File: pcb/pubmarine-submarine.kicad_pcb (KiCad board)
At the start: 2 copper layers, 150.5 x 100 mm, 68 parts, among them J1 GPIO_IN, J10 RPD, J11 Screw_Terminal_01x08, J12 Screw_Terminal_01x08, J13 ADC_HDR, J14 PWM_HDR, J2 GPIO_OUT, J3 FYL, J4 FYR, J5 FPU, J6 FPD, J7 RPU, J8 RYL, J9 RYR, Q1 AO3400A, Q2 AO3400A, Q3 AO3400A, Q4 AO3400A, Q5 AO3400A, Q6 AO3400A, Q7 AO3400A, Q8 AO3400A, U1 A4950E, U2 A4950E, U3 A4950E, U4 A4950E, U5 TLC5947DAP, U6 MCP3008

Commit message: new PCB
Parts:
- added C10: 0.22uF, Capacitor_SMD:C_0603_1608Metric_Pad1.08x0.95mm_HandSolder, F.Cu at (254.5, 69.8)
- added C11: 100uF, Capacitor_THT:CP_Radial_D6.3mm_P2.50mm, F.Cu at (257.8, 84.5)
- added C9: 100uF, Capacitor_THT:CP_Radial_D6.3mm_P2.50mm, F.Cu at (248.5, 84.5)
- added D10: WS2812B, LED_SMD:LED_WS2812B_PLCC4_5.0x5.0mm_P3.2mm, F.Cu at (271.1, 82.0)
- added D11: WS2812B, LED_SMD:LED_WS2812B_PLCC4_5.0x5.0mm_P3.2mm, F.Cu at (270.9, 91.0)
- added D12: LED, LED_SMD:LED_0603_1608Metric_Pad1.05x0.95mm_HandSolder, F.Cu at (199.0, 79.2)
- added D13: LED, LED_SMD:LED_0603_1608Metric_Pad1.05x0.95mm_HandSolder, F.Cu at (212.2, 79.0)
- added D14: LED, LED_SMD:LED_0603_1608Metric_Pad1.05x0.95mm_HandSolder, F.Cu at (223.9, 79.0)
- added D9: WS2812B, LED_SMD:LED_WS2812B_PLCC4_5.0x5.0mm_P3.2mm, F.Cu at (271.1, 72.5)
- added J15: Servo1, Connector_JST:JST_PH_B3B-PH-K_1x03_P2.00mm_Vertical, F.Cu at (272.5, 114.8)
- added J16: Servo2, Connector_JST:JST_PH_B3B-PH-K_1x03_P2.00mm_Vertical, F.Cu at (272.5, 109.3)
- added J17: Servo3, Connector_JST:JST_PH_B3B-PH-K_1x03_P2.00mm_Vertical, F.Cu at (272.5, 103.8)
- added J18: Servo4, Connector_JST:JST_PH_B3B-PH-K_1x03_P2.00mm_Vertical, F.Cu at (272.5, 98.2)
- added J19: Conn_01x02, Connector_JST:JST_XH_B2B-XH-AM_1x02_P2.50mm_Vertical, F.Cu at (235.9, 63.0)
- added J20: Conn_01x02, Connector_JST:JST_XH_B2B-XH-AM_1x02_P2.50mm_Vertical, F.Cu at (244.7, 63.0)
- added J21: Conn_01x02, Connector_JST:JST_XH_B2B-XH-AM_1x02_P2.50mm_Vertical, F.Cu at (253.4, 63.0)
- added J22: Conn_01x02, Connector_JST:JST_XH_B2B-XH-AM_1x02_P2.50mm_Vertical, F.Cu at (262.4, 63.0)
- added J23: Conn_01x02, Connector_JST:JST_PH_B2B-PH-K_1x02_P2.00mm_Vertical, F.Cu at (178.2, 79.8)
- added J24: Conn_01x02, Connector_JST:JST_PH_B2B-PH-K_1x02_P2.00mm_Vertical, F.Cu at (185.5, 79.8)
- added R21: 1K, Resistor_SMD:R_0603_1608Metric_Pad0.98x0.95mm_HandSolder, F.Cu at (194.8, 79.2)
- added R22: 330, Resistor_SMD:R_0603_1608Metric_Pad0.98x0.95mm_HandSolder, F.Cu at (207.8, 79.0)
- added R23: 330, Resistor_SMD:R_0603_1608Metric_Pad0.98x0.95mm_HandSolder, F.Cu at (219.6, 79.0)
- added SW1: SW_SPDT, Button_Switch_THT:SW_Slide_SPDT_Straight_CK_OS102011MS2Q, F.Cu at (199.1, 75.0)
- added SW2: SW_SPDT, Button_Switch_THT:SW_Slide_SPDT_Straight_CK_OS102011MS2Q, F.Cu at (211.6, 75.0)
- added SW3: SW_SPDT, Button_Switch_THT:SW_Slide_SPDT_Straight_CK_OS102011MS2Q, F.Cu at (223.7, 75.0)
- C1, C5, C7: value 0.22uF -> 100uF; footprint Capacitor_SMD:C_0603_1608Metric_Pad1.08x0.95mm_HandSolder -> Capacitor_THT:CP_Radial_D6.3mm_P2.50mm
- C2: footprint Capacitor_THT:CP_Radial_D5.0mm_P2.50mm -> Capacitor_THT:CP_Radial_D6.3mm_P2.50mm
- C3: value 0.22uF -> 0.1uF
- C4, C6, C8: value 100uF -> 0.22uF; footprint Capacitor_THT:CP_Radial_D5.0mm_P2.50mm -> Capacitor_SMD:C_0603_1608Metric_Pad1.08x0.95mm_HandSolder
- D1, D2, D3, D4, D5, D6, D7, D8: value D_Schottky -> 1N5822; footprint Diode_SMD:D_0603_1608Metric_Pad1.05x0.95mm_HandSolder -> Diode_SMD:D_0603_1608Metric
- H1: value MountingHole_Pad -> MountingHole; footprint MountingHole:MountingHole_3.2mm_M3_Pad -> MountingHole:MountingHole_2.2mm_M2
- H2, H3: footprint MountingHole:MountingHole_3.2mm_M3 -> MountingHole:MountingHole_2.2mm_M2
- H4: value MountingHole -> MountingHole_Pad; footprint MountingHole:MountingHole_3.2mm_M3 -> MountingHole:MountingHole_2.2mm_M2_Pad
- J1: value GPIO_IN -> Screw_Terminal_01x02; footprint Connector_PinHeader_2.54mm:PinHeader_2x20_P2.54mm_Vertical -> TerminalBlock:TerminalBlock_Altech_AK300-2_P5.00mm
- J10: value RPD -> Conn_01x02
- J11: value Screw_Terminal_01x08 -> Conn_01x02; footprint TerminalBlock_Phoenix:TerminalBlock_Phoenix_MKDS-1,5-8_1x08_P5.00mm_Horizontal -> Connector_JST:JST_PH_B2B-PH-K_1x02_P2.00mm_Vertical
- J12: value Screw_Terminal_01x08 -> Screw_Terminal_01x02; footprint TerminalBlock_Phoenix:TerminalBlock_Phoenix_MKDS-1,5-8_1x08_P5.00mm_Horizontal -> TerminalBlock:TerminalBlock_Altech_AK300-2_P5.00mm
- J13: value ADC_HDR -> Conn_01x03; footprint Connector_PinHeader_2.54mm:PinHeader_1x08_P2.54mm_Vertical -> Connector_JST:JST_PH_B3B-PH-K_1x03_P2.00mm_Vertical
- J14: value PWM_HDR -> Conn_01x04; footprint Connector_PinHeader_2.54mm:PinHeader_1x08_P2.54mm_Vertical -> Connector_JST:JST_PH_B4B-PH-K_1x04_P2.00mm_Vertical
- J2: value GPIO_OUT -> Conn_01x02; footprint Connector_PinHeader_2.54mm:PinHeader_2x20_P2.54mm_Vertical -> Connector_JST:JST_PH_B2B-PH-K_1x02_P2.00mm_Vertical
- J3: value FYL -> Conn_01x02
- J4: value FYR -> Conn_01x02
- J5: value FPU -> Conn_01x02
- J6: value FPD -> Screw_Terminal_01x02; footprint Connector_JST:JST_PH_B2B-PH-K_1x02_P2.00mm_Vertical -> TerminalBlock:TerminalBlock_Altech_AK300-2_P5.00mm
- J7: value RPU -> Screw_Terminal_01x02; footprint Connector_JST:JST_PH_B2B-PH-K_1x02_P2.00mm_Vertical -> TerminalBlock:TerminalBlock_Altech_AK300-2_P5.00mm
- J8: value RYL -> Conn_01x02
- J9: value RYR -> Conn_01x02
- Q1, Q2, Q3, Q4, Q5, Q6, Q7, Q8: value AO3400A -> Q_NMOS_Depletion_DGS; footprint Package_TO_SOT_SMD:SOT-23 -> Package_TO_SOT_SMD:SOT-223-3_TabPin2
- R1, R2, R3, R4: value 1.1Ω -> 470; footprint Resistor_SMD:R_1812_4532Metric_Pad1.30x3.40mm_HandSolder -> Resistor_SMD:R_0603_1608Metric_Pad0.98x0.95mm_HandSolder
- R10, R12: value 100 -> 470
- R11, R9: value 1K -> 470
- R13, R15, R6, R7: value 1K -> 10k
- R14, R16, R5, R8: value 100 -> 10k
- R17: value 1K -> 4.7K
- R18: value 100 -> 4.7K
- R19: value 1K -> 10K
- R20: value 100 -> 20K
- U1: value A4950E -> Pico; footprint Package_SO:SOIC-8-1EP_3.9x4.9mm_P1.27mm_EP2.41x3.3mm -> MCU_RaspberryPi_and_Boards:RPi_Pico_SMD_TH
- U2: value A4950E -> SN74LV1T34DBV; footprint Package_SO:SOIC-8-1EP_3.9x4.9mm_P1.27mm_EP2.41x3.3mm -> Package_TO_SOT_SMD:SOT-23-5
- U3, U4: footprint Package_SO:SOIC-8-1EP_3.9x4.9mm_P1.27mm_EP2.41x3.3mm -> Package_SO:SOIC-8-1EP_3.9x4.9mm_P1.27mm_EP2.62x3.51mm_ThermalVias
- U5: value TLC5947DAP -> A4950E; footprint Package_SO:HTSSOP-32-1EP_6.1x11mm_P0.65mm_EP5.2x11mm_Mask4.11x4.36mm_ThermalVias -> Package_SO:SOIC-8-1EP_3.9x4.9mm_P1.27mm_EP2.62x3.51mm_ThermalVias
- U6: value MCP3008 -> A4950E; footprint Package_SO:SOIC-16_3.9x9.9mm_P1.27mm -> Package_SO:SOIC-8-1EP_3.9x4.9mm_P1.27mm_EP2.62x3.51mm_ThermalVias
- moved H1 198.3 mm to (272.0, 63.0)
- moved J11 170.4 mm to (254.8, 135.2)
- moved J14 148.4 mm to (266.5, 119.5)
- moved J2 131.6 mm to (191.0, 135.4)
- moved J13 123.0 mm to (268.5, 125.2)
- moved J1 112.5 mm to (200.0, 65.5), turned to 180 degrees
- moved H2 110.1 mm to (271.5, 134.5)
- moved J8 109.0 mm to (232.2, 135.2)
- moved J9 109.0 mm to (239.8, 135.2)
- moved Q8 108.6 mm to (255.6, 125.2)
- moved J5 108.3 mm to (213.5, 135.4)
- moved J4 108.3 mm to (206.0, 135.4)
- moved J3 108.2 mm to (198.5, 135.4)
- moved U5 108.1 mm to (247.8, 75.0), turned to 90 degrees
- moved J10 105.3 mm to (247.2, 135.2)
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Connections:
- C1 pad 1: +12VA -> +5VP
- C1 pad 2: GNDA -> GND
- C2 pad 1: +12VA -> +5VP
- C2 pad 2: GNDA -> GND
- C3 pad 1: +12VA -> +5VL
- C3 pad 2: GNDA -> GND
- C4 pad 1: +12VA -> +12V
- C4 pad 2: GNDA -> GND
- C5 pad 1: +12VA -> +12V
- C5 pad 2: GNDA -> GND
- C6 pad 1: +12VA -> +12V
- C6 pad 2: GNDA -> GND
- C7 pad 1: +12VA -> +12V
- C7 pad 2: GNDA -> GND
- C8 pad 1: +12VA -> +12V
- C8 pad 2: GNDA -> GND
- D1 pad 1: +12VA -> +5VP
- D1 pad 2: FYL- -> /FU-
- D2 pad 1: +12VA -> +5VP
- D2 pad 2: FYR- -> /FD-
- D3 pad 1: +12VA -> +5VP
- D3 pad 2: FPU- -> /FL-
- D4 pad 1: +12VA -> +5VP
- D4 pad 2: FPD- -> /FR-
- D5 pad 1: +12VA -> +5VP
- D5 pad 2: RYL- -> /RU-
- D6 pad 1: +12VA -> +5VP
- D6 pad 2: RYR- -> /RD-
- D7 pad 1: +12VA -> +5VP
- D7 pad 2: RPU- -> /RL-
- D8 pad 1: +12VA -> +5VP
- D8 pad 2: RPD- -> /RR-
- J1 pad 1: unconnected-(J1-3V3-Pad1) -> Net-(J1-Pin_1)
- J1 pad 2: +5VD -> GND
- J10 pad 1: +12VA -> +5VP
- J10 pad 2: RPD- -> /RL-
- J11 pad 1: +12VA -> +5VP
- J11 pad 2: GNDA -> /RR-
- J12 pad 1: X+ -> +5VL
- J12 pad 2: X- -> GND
- J13 pad 1: CH0 -> GND
- J13 pad 2: CH1 -> +5VL
- J13 pad 3: CH2 -> Net-(J13-Pin_3)
- J14 pad 1: PWM16 -> GND
- J14 pad 2: PWM17 -> +5VL
- J14 pad 3: PWM18 -> SDA
- J14 pad 4: PWM19 -> SCL
- J2 pad 1: unconnected-(J2-3V3-Pad1) -> +5VP
- J2 pad 2: +5VD -> /FU-
- J3 pad 1: +12VA -> +5VP
- J3 pad 2: FYL- -> /FD-
- J4 pad 1: +12VA -> +5VP
- J4 pad 2: FYR- -> /FL-
- J5 pad 1: +12VA -> +5VP
- J5 pad 2: FPU- -> /FR-
- J6 pad 1: +12VA -> Net-(J6-Pin_1)
- J6 pad 2: FPD- -> GND
- J7 pad 1: +12VA -> Net-(J7-Pin_1)
- J7 pad 2: RPU- -> GND
- J8 pad 1: +12VA -> +5VP
- J8 pad 2: RYL- -> /RU-
- J9 pad 1: +12VA -> +5VP
- J9 pad 2: RYR- -> /RD-
- Q1 pad 1: Net-(Q1-G) -> /FU-
- Q1 pad 2: GND -> Net-(Q1-G)
- Q1 pad 3: FYL- -> GND
- Q2 pad 1: Net-(Q2-G) -> /FD-
- Q2 pad 2: GND -> Net-(Q2-G)
- Q2 pad 3: FYR- -> GND
- Q3 pad 1: Net-(Q3-G) -> /FL-
- Q3 pad 2: GND -> Net-(Q3-G)
- Q3 pad 3: FPU- -> GND
- Q4 pad 1: Net-(Q4-G) -> /FR-
- Q4 pad 2: GND -> Net-(Q4-G)
- Q4 pad 3: FPD- -> GND
- Q5 pad 1: Net-(Q5-G) -> /RU-
- Q5 pad 2: GND -> Net-(Q5-G)
- Q5 pad 3: RYL- -> GND
- Q6 pad 1: Net-(Q6-G) -> /RD-
- Q6 pad 2: GND -> Net-(Q6-G)
- Q6 pad 3: RYR- -> GND
- Q7 pad 1: Net-(Q7-G) -> /RL-
- Q7 pad 2: GND -> Net-(Q7-G)
- Q7 pad 3: RPU- -> GND
- Q8 pad 1: Net-(Q8-G) -> /RR-
- Q8 pad 2: GND -> Net-(Q8-G)
- Q8 pad 3: RPD- -> GND
- R1 pad 1: Net-(U1-LSS) -> FU
- R1 pad 2: GNDA -> Net-(Q1-G)
- R10 pad 1: PWM10 -> RD
- R10 pad 2: Net-(Q3-G) -> Net-(Q6-G)
- R11 pad 1: PWM11 -> RL
- R11 pad 2: GND -> Net-(Q7-G)
- R12 pad 1: PWM11 -> RR
- R12 pad 2: Net-(Q4-G) -> Net-(Q8-G)
- R13 pad 1: PWM12 -> Net-(Q5-G)
- R14 pad 1: PWM12 -> Net-(Q6-G)
- R14 pad 2: Net-(Q5-G) -> GND
- R15 pad 1: PWM13 -> Net-(Q7-G)
- R16 pad 1: PWM13 -> Net-(Q8-G)
- R16 pad 2: Net-(Q6-G) -> GND
- R17 pad 1: PWM14 -> SDA
- R17 pad 2: GND -> +5VL
- R18 pad 1: PWM14 -> SCL
- R18 pad 2: Net-(Q7-G) -> +5VL
- R19 pad 1: PWM15 -> Net-(J13-Pin_3)
- R19 pad 2: GND -> SENS1
- R2 pad 1: Net-(U2-LSS) -> FD
- R2 pad 2: GNDA -> Net-(Q2-G)
- R20 pad 1: PWM15 -> SENS1
- R20 pad 2: Net-(Q8-G) -> GND
- R3 pad 1: Net-(U3-LSS) -> FL
- R3 pad 2: GNDA -> Net-(Q3-G)
- R4 pad 1: Net-(U4-LSS) -> FR
- R4 pad 2: GNDA -> Net-(Q4-G)
- R5 pad 1: PWM8 -> Net-(Q1-G)
- R5 pad 2: Net-(Q1-G) -> GND
- R6 pad 1: PWM8 -> Net-(Q2-G)
- R7 pad 1: PWM9 -> Net-(Q3-G)
- R8 pad 1: PWM9 -> Net-(Q4-G)
- R8 pad 2: Net-(Q2-G) -> GND
- R9 pad 1: PWM10 -> RU
- R9 pad 2: GND -> Net-(Q5-G)
- U1 pad 1: GNDA -> LED_DATA
- U1 pad 2: unconnected-(U1-IN2-Pad2) -> IN_W2
- U1 pad 3: unconnected-(U1-IN1-Pad3) -> GND
- U1 pad 4: +3V3 -> SDA
- U1 pad 5: +12VA -> SCL
- U1 pad 6: X+ -> FU
- U1 pad 7: Net-(U1-LSS) -> FD
- U1 pad 8: X- -> GND
- U1 pad 9: GNDA -> FL
- U2 pad 1: GNDA -> unconnected-(U2-NC-Pad1)
- U2 pad 2: unconnected-(U2-IN2-Pad2) -> LED_DATA
- U2 pad 3: unconnected-(U2-IN1-Pad3) -> GND
- U2 pad 4: +3V3 -> Net-(D9-DIN)
- U2 pad 5: +12VA -> +5VL
- U3 pad 1: GNDA -> GND
- U3 pad 2: unconnected-(U3-IN2-Pad2) -> IN_X2
- U3 pad 3: unconnected-(U3-IN1-Pad3) -> IN_X1
- U3 pad 4: +3V3 -> +3.3V
- U3 pad 5: +12VA -> +12V
- U3 pad 6: X+ -> /X+
- U3 pad 7: Net-(U3-LSS) -> unconnected-(U3-LSS-Pad7)
- U3 pad 8: X- -> /X-
- U3 pad 9: GNDA -> GND
- U4 pad 1: GNDA -> GND
- U4 pad 2: unconnected-(U4-IN2-Pad2) -> IN_Y2
- U4 pad 3: unconnected-(U4-IN1-Pad3) -> IN_Y1
- U4 pad 4: +3V3 -> +3.3V
- U4 pad 5: +12VA -> +12V
- U4 pad 6: X+ -> /Y+
- U4 pad 7: Net-(U4-LSS) -> unconnected-(U4-LSS-Pad7)
- U4 pad 8: X- -> /Y-
- U4 pad 9: GNDA -> GND
- U5 pad 2: unconnected-(U5-BLANK-Pad2) -> IN_Z2
- U5 pad 3: unconnected-(U5-SCLK-Pad3) -> IN_Z1
- U5 pad 4: unconnected-(U5-SIN-Pad4) -> +3.3V
- U5 pad 5: PWM0 -> +12V
- U5 pad 6: PWM1 -> /Z+
- U5 pad 7: PWM2 -> unconnected-(U5-LSS-Pad7)
- U5 pad 8: PWM3 -> /Z-
- U5 pad 9: PWM4 -> GND
- U6 pad 1: CH0 -> GND
- U6 pad 2: CH1 -> IN_W2
- U6 pad 3: CH2 -> IN_W1
- U6 pad 4: CH3 -> +3.3V
- U6 pad 5: CH4 -> +12V
- U6 pad 6: CH5 -> /W+
- U6 pad 7: CH6 -> unconnected-(U6-LSS-Pad7)
- U6 pad 8: CH7 -> /W-
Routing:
- removed copper zone on B.Cu, net GND
- removed copper zone on F.Cu, net GND
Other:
- board size 150.5 x 100 mm -> 100 x 80 mm
- board text removed: "${65d5fb20-c9c2-4316-b874-62329deea464:SHORT_NET_NAME(1)}"
- board text removed: "${65d5fb20-c9c2-4316-b874-62329deea464:SHORT_NET_NAME(2)}"
- board text removed: "${65d5fb20-c9c2-4316-b874-62329deea464:SHORT_NET_NAME(3)}"
- board text removed: "${65d5fb20-c9c2-4316-b874-62329deea464:SHORT_NET_NAME(4)}"
- board text removed: "${65d5fb20-c9c2-4316-b874-62329deea464:SHORT_NET_NAME(5)}"
- board text removed: "${65d5fb20-c9c2-4316-b874-62329deea464:SHORT_NET_NAME(6)}"
- board text removed: "${65d5fb20-c9c2-4316-b874-62329deea464:SHORT_NET_NAME(7)}"
- board text removed: "${65d5fb20-c9c2-4316-b874-62329deea464:SHORT_NET_NAME(8)}"
- board text removed: "${f41ea258-c64d-4c3b-b979-3761c3714b82:SHORT_NET_NAME(1)}"
- board text removed: "${f41ea258-c64d-4c3b-b979-3761c3714b82:SHORT_NET_NAME(2)}"
- board text removed: "${f41ea258-c64d-4c3b-b979-3761c3714b82:SHORT_NET_NAME(3)}"
- board text removed: "${f41ea258-c64d-4c3b-b979-3761c3714b82:SHORT_NET_NAME(4)}"
- board text removed: "${f41ea258-c64d-4c3b-b979-3761c3714b82:SHORT_NET_NAME(5)}"
- board text removed: "${f41ea258-c64d-4c3b-b979-3761c3714b82:SHORT_NET_NAME(6)}"
- board text removed: "${f41ea258-c64d-4c3b-b979-3761c3714b82:SHORT_NET_NAME(7)}"
- board text removed: "${f41ea258-c64d-4c3b-b979-3761c3714b82:SHORT_NET_NAME(8)}"

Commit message: pcb updates
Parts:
- removed SW3: SW_SPDT, Button_Switch_THT:SW_Slide_SPDT_Straight_CK_OS102011MS2Q
- added D15: LED, LED_SMD:LED_0603_1608Metric_Pad1.05x0.95mm_HandSolder, F.Cu at (60.0, 44.5)
- added D16: LED, LED_SMD:LED_0603_1608Metric_Pad1.05x0.95mm_HandSolder, F.Cu at (125.0, 117.0)
- added J25: Conn_01x20, Connector_PinHeader_2.54mm:PinHeader_1x20_P2.54mm_Vertical, F.Cu at (52.9, 97.0)
- added J26: Conn_01x20, Connector_PinHeader_2.54mm:PinHeader_1x20_P2.54mm_Vertical, F.Cu at (52.9, 69.0)
- added J27: Conn_01x03, Connector_PinHeader_2.54mm:PinHeader_1x03_P2.54mm_Vertical, F.Cu at (106.0, 85.5)
- added R24: R, Resistor_SMD:R_0603_1608Metric_Pad0.98x0.95mm_HandSolder, F.Cu at (109.1, 59.0)
- added R25: R, Resistor_SMD:R_0603_1608Metric_Pad0.98x0.95mm_HandSolder, F.Cu at (113.1, 59.0)
- added R26: 330, Resistor_SMD:R_0603_1608Metric_Pad0.98x0.95mm_HandSolder, F.Cu at (62.0, 44.5)
- added R27: 1K, Resistor_SMD:R_0603_1608Metric_Pad0.98x0.95mm_HandSolder, F.Cu at (125.1, 115.0)
- moved U3 167.0 mm to (68.5, 57.8)
- moved J22 167.0 mm to (96.5, 44.0)
- moved J21 166.5 mm to (88.0, 44.0)
- moved J20 166.3 mm to (79.5, 44.0)
- moved J19 166.0 mm to (71.0, 44.0)
- moved C11 165.6 mm to (96.0, 49.0), turned to -90 degrees
- moved U4 165.1 mm to (77.0, 57.8)
- moved C9 164.9 mm to (87.5, 49.0), turned to -90 degrees
- moved C7 164.4 mm to (79.0, 49.0), turned to -90 degrees
- moved C5 163.7 mm to (70.5, 49.0), turned to -90 degrees
- moved C4 163.3 mm to (72.0, 56.1), turned to -90 degrees
- moved U5 163.2 mm to (85.5, 57.8)
- moved C6 161.4 mm to (80.5, 56.1), turned to -90 degrees
- moved U6 161.3 mm to (94.0, 57.8)
- moved C8 159.6 mm to (89.0, 56.1), turned to -90 degrees
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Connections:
- net /W+ renamed /WA
- net /W- renamed /WB
- net /X+ renamed /XA
- net /X- renamed /XB
- net /Y+ renamed /YA
- net /Y- renamed /YB
- net /Z+ renamed /ZA
- net /Z- renamed /ZB
- J1 pad 1: Net-(J1-Pin_1) -> +12V
- J12 pad 1: +5VL -> /PI_PWR
- J23 pad 1: +5VP -> /LED_PWR
- J24 pad 1: +5VP -> /LED_PWR
- J6 pad 1: Net-(J6-Pin_1) -> +5VP
- J7 pad 1: Net-(J7-Pin_1) -> +5VL
- SW1 pad 2: Net-(J1-Pin_1) -> /PI_PWR
- SW1 pad 3: +12V -> +5VL
- SW2 pad 2: Net-(J6-Pin_1) -> /LED_PWR
- SW2 pad 3: +5VP -> +12V
- U1 pad 16: SV1 -> SV4
- U1 pad 17: SV2 -> SV3
- U1 pad 19: SV3 -> SV2
- U1 pad 2: IN_W2 -> IN_W1
- U1 pad 20: SV4 -> SV1
- U1 pad 21: IN_X1 -> IN_W2
- U1 pad 22: IN_X2 -> IN_Z1
- U1 pad 24: IN_Y1 -> IN_Z2
- U1 pad 25: IN_Y2 -> IN_Y1
- U1 pad 26: IN_Z1 -> IN_Y2
- U1 pad 27: IN_Z2 -> IN_X1
- U1 pad 29: IN_W1 -> IN_X2
- U1 pad 30: unconnected-(U1-RUN-Pad30)_1 -> /RUN
- U1 pad 34: unconnected-(U1-GPIO28_ADC2-Pad34) -> /GPIO28_ADC2
- U1 pad 35: unconnected-(U1-ADC_VREF-Pad35)_1 -> /ADC_VREF
- U1 pad 37: unconnected-(U1-3V3_EN-Pad37) -> Net-(J26-Pin_4)
- U1 pad 40: unconnected-(U1-VBUS-Pad40)_1 -> /VBUS
- U1 pad 41: unconnected-(U1-SWCLK-Pad41)_1 -> Net-(J27-Pin_1)
- U1 pad 43: unconnected-(U1-SWDIO-Pad43) -> Net-(J27-Pin_3)
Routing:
- net +5VL: track 0.00 -> 201.4 mm, vias 0 -> 2
- net +12V: track 0.00 -> 82.8 mm
- net IN_W1: track 0.00 -> 78.6 mm
- net +5VP: track 0.00 -> 69.9 mm
- net SV4: track 0.00 -> 64.2 mm
- net SV3: track 0.00 -> 57.4 mm
- net +3.3V: track 0.00 -> 56.4 mm, vias 0 -> 4
- net SV2: track 0.00 -> 50.1 mm
- net SV1: track 0.00 -> 49.1 mm
- net IN_X1: track 0.00 -> 26.3 mm
- net /LED_PWR: track 0.00 -> 24.8 mm
- net IN_Y1: track 0.00 -> 23.2 mm
- net IN_X2: track 0.00 -> 22.6 mm
- net IN_Z1: track 0.00 -> 22.3 mm
- net /PI_PWR: track 0.00 -> 21.7 mm
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- added copper zone on B.Cu, net GND
- added copper zone on F.Cu, net GND
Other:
- board size 100 x 80 mm -> 225.5 x 99 mm
- board text added: "1"
- board text added: "2"
- board text added: "3"
- board text added: "4"
- board text added: "5VL"
- board text added: "5VP"
- board text added: "ADC_VREF"
- board text added: "BLINKENLIGHTS"
- board text added: "I2C Pullups"
- board text added: "SERVOS"
- board text added: "VBAT"
- board text added: "W"
- board text added: "X"
- board text added: "Y"
- board text added: "Z"

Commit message: pcb update
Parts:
- Q1, Q2, Q3, Q4, Q5, Q6, Q7, Q8: value Q_NMOS_Depletion_DGS -> AO3400A; footprint Package_TO_SOT_SMD:SOT-223-3_TabPin2 -> Package_TO_SOT_SMD:SOT-23_Handsoldering
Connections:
- Q1 pad 1: /FU- -> Net-(Q1-G)
- Q1 pad 2: Net-(Q1-G) -> GND
- Q1 pad 3: GND -> /FU-
- Q2 pad 1: /FD- -> Net-(Q2-G)
- Q2 pad 2: Net-(Q2-G) -> GND
- Q2 pad 3: GND -> /FD-
- Q3 pad 1: /FL- -> Net-(Q3-G)
- Q3 pad 2: Net-(Q3-G) -> GND
- Q3 pad 3: GND -> /FL-
- Q4 pad 1: /FR- -> Net-(Q4-G)
- Q4 pad 2: Net-(Q4-G) -> GND
- Q4 pad 3: GND -> /FR-
- Q5 pad 1: /RU- -> Net-(Q5-G)
- Q5 pad 2: Net-(Q5-G) -> GND
- Q5 pad 3: GND -> /RU-
- Q6 pad 1: /RD- -> Net-(Q6-G)
- Q6 pad 2: Net-(Q6-G) -> GND
- Q6 pad 3: GND -> /RD-
- Q7 pad 1: /RL- -> Net-(Q7-G)
- Q7 pad 2: Net-(Q7-G) -> GND
- Q7 pad 3: GND -> /RL-
- Q8 pad 1: /RR- -> Net-(Q8-G)
- Q8 pad 2: Net-(Q8-G) -> GND
- Q8 pad 3: GND -> /RR-

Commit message: pcb updates
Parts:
- moved Q8 141.8 mm to (114.8, 108.5), turned to -90 degrees
- moved R16 141.7 mm to (117.2, 110.0), turned to -90 degrees
- moved D8 140.6 mm to (115.0, 113.0)
- moved R15 139.3 mm to (110.2, 110.0), turned to -90 degrees
- moved Q7 139.2 mm to (107.8, 108.5), turned to -90 degrees
- moved D7 138.1 mm to (108.0, 113.0)
- moved R14 136.8 mm to (103.2, 110.0), turned to -90 degrees
- moved Q6 136.6 mm to (100.8, 108.5), turned to -90 degrees
- moved R12 136.3 mm to (117.2, 106.4), turned to -90 degrees
- moved D6 135.4 mm to (101.0, 113.0)
- moved R9 134.2 mm to (96.2, 106.4), turned to -90 degrees
- moved Q5 134.1 mm to (93.8, 108.5), turned to -90 degrees
- moved R11 133.5 mm to (110.2, 106.4), turned to -90 degrees
- moved D5 133.1 mm to (94.0, 113.0)
- moved R8 131.5 mm to (86.2, 110.0), turned to -90 degrees
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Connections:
- R17 pad 2: +5VL -> +3.3V
- R18 pad 2: +5VL -> +3.3V
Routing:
- net +5VP: track 69.9 -> 291.4 mm, vias 0 -> 9
- net LED_DATA: track 5.11 -> 101.8 mm, vias 0 -> 1
- net SENS1: track 7.11 -> 86.7 mm, vias 0 -> 3
- net SCL: track 10.3 -> 88.3 mm, vias 0 -> 1
- net SDA: track 13.1 -> 90.9 mm, vias 0 -> 1
- net +12V: track 82.8 -> 155.0 mm, vias 0 -> 1
- net +3.3V: track 56.4 -> 127.4 mm, vias 4 -> 5
- net BAT_SENS: track 7.29 -> 52.5 mm, vias 0 -> 1
- net RR: track 5.11 -> 37.5 mm
- net RL: track 5.11 -> 33.0 mm
- net RD: track 5.11 -> 31.1 mm
- net RU: track 5.11 -> 26.6 mm
- net FR: track 5.11 -> 19.1 mm
- net FL: track 5.11 -> 16.1 mm
- net FD: track 5.11 -> 15.3 mm
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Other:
- board size 225.5 x 99 mm -> 100 x 80 mm
- board text added: "+"
- board text added: "-"
- board text added: "12V"
- board text added: "FD"
- board text added: "FL"
- board text added: "FR"
- board text added: "FU"
- board text added: "Fl"
- board text added: "I2C"
- board text added: "LED"
- board text added: "RD"
- board text added: "RL"
- board text added: "RPi"
- board text added: "RR"
- board text added: "RU"
- board text added: "SCL"
- board text added: "SDA"
- board text added: "SENS"
- board text added: "SV1"
- board text added: "SV2"
- board text added: "SV3"
- board text added: "SV4"
- board text added: "The PubSubHub revision 1.0 by @DeltaWhy https://github.com/PubmarineSubmarine JLCJLCJLCJLC"

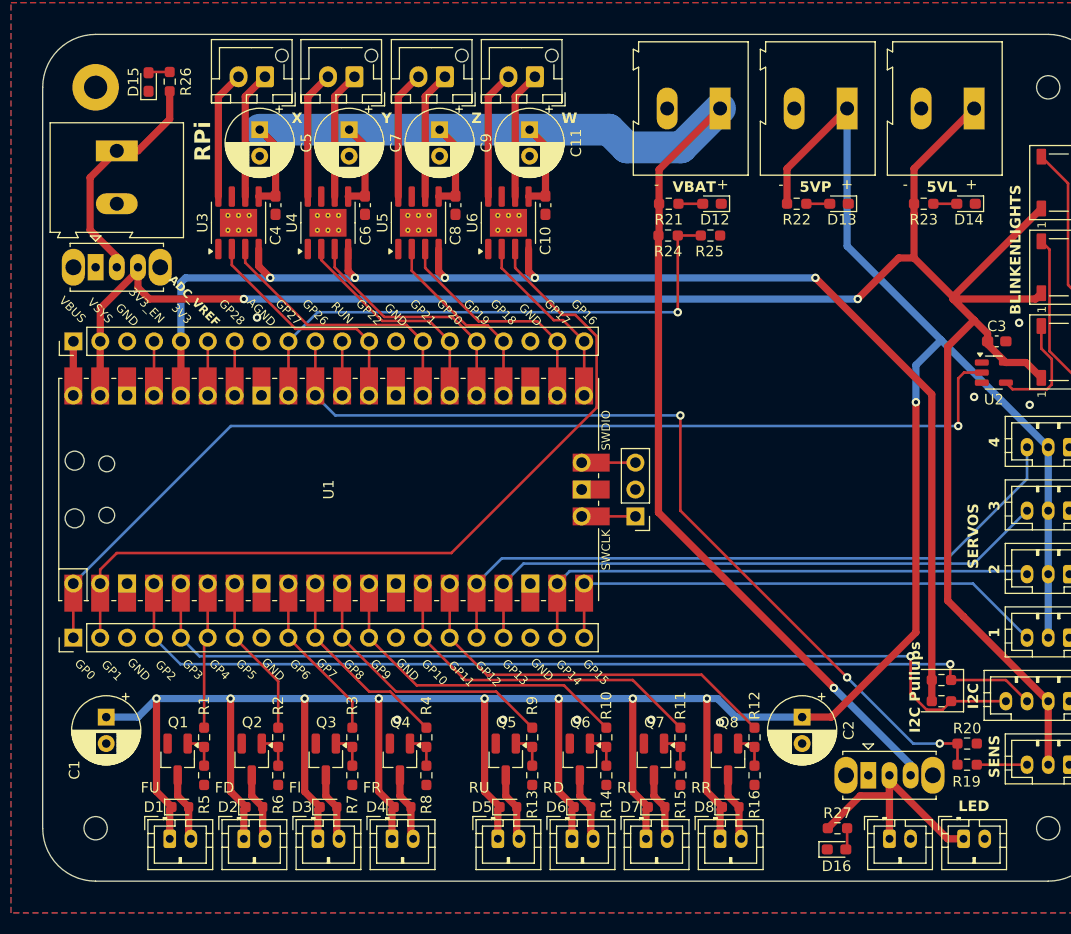
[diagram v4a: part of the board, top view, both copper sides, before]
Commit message: pcb: IMU breakout and silkscreen cleanup
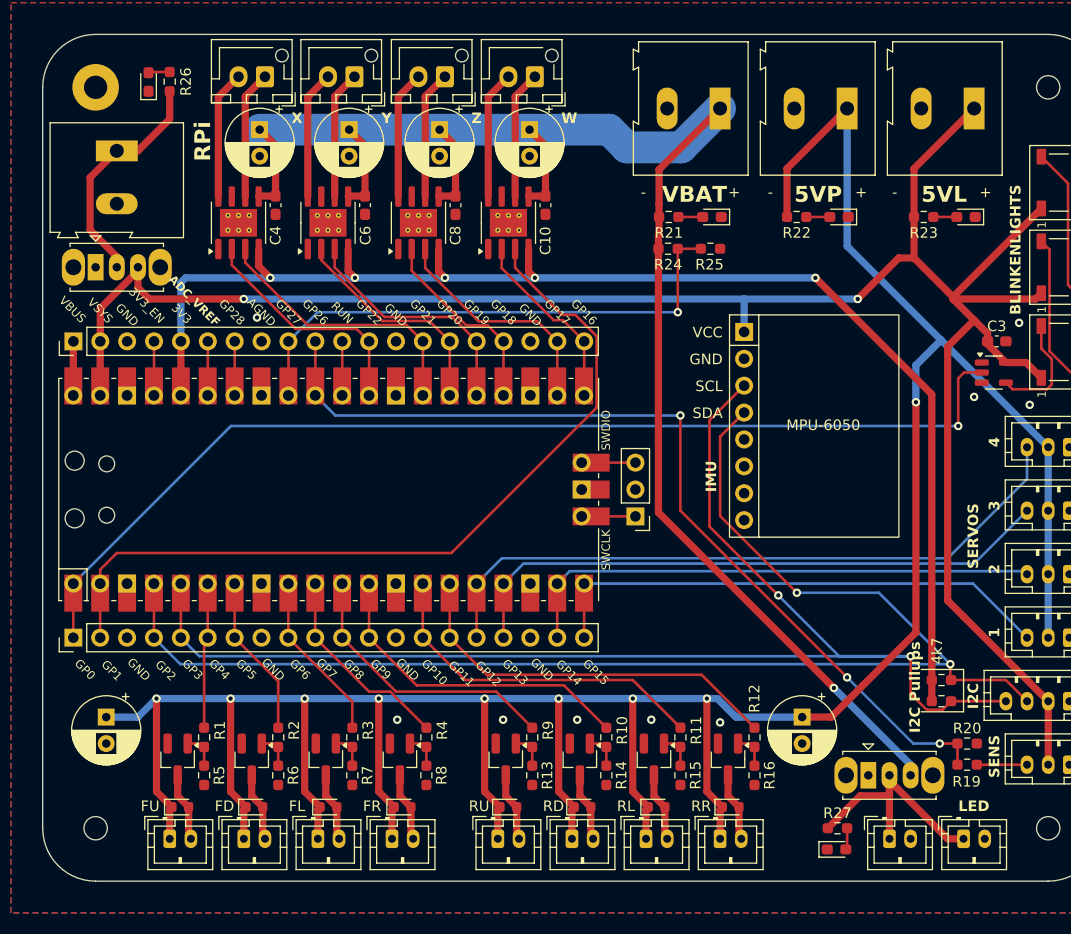
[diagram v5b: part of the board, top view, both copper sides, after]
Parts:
- added U7: MPU-6050, pubmarine-submarine:MPU-6050_Module, F.Cu at (116.3, 68.1)
- R24: value R -> 39k
- R25: value R -> 13k
- moved D12 1.25 mm to (113.2, 57.2)
- moved D13 1.25 mm to (125.2, 57.2)
- moved D14 1.25 mm to (137.2, 57.2)
- moved R21 1.25 mm to (109.1, 57.2)
- moved R22 1.25 mm to (121.2, 57.2)
- moved R23 1.25 mm to (133.2, 57.2)
- moved R24 1.25 mm to (109.1, 60.2)
- moved R25 1.25 mm to (113.1, 60.2)
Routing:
- net SCL: track 88.3 -> 127.0 mm, vias 1 -> 2
- net SDA: track 90.9 -> 129.2 mm, vias 1 -> 2
- net +5VL: track 192.1 -> 195.3 mm
- net BAT_SENS: track 52.5 -> 51.2 mm
- net +5VP: track 291.4 -> 292.6 mm
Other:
- board text added: "4k7"
- board text added: "IMU"
- board text added: "MPU-6050"
- board text removed: "Fl"

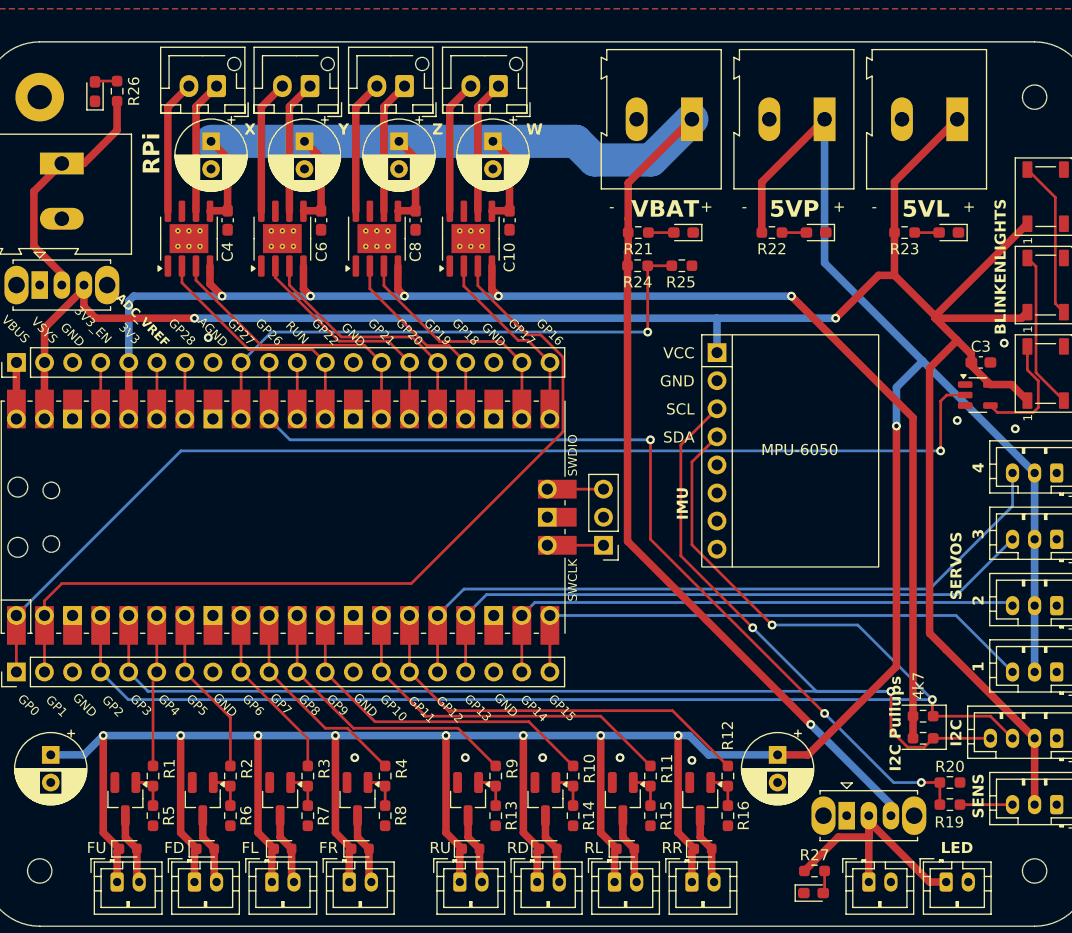
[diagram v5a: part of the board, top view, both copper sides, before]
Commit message: silkscreen updates
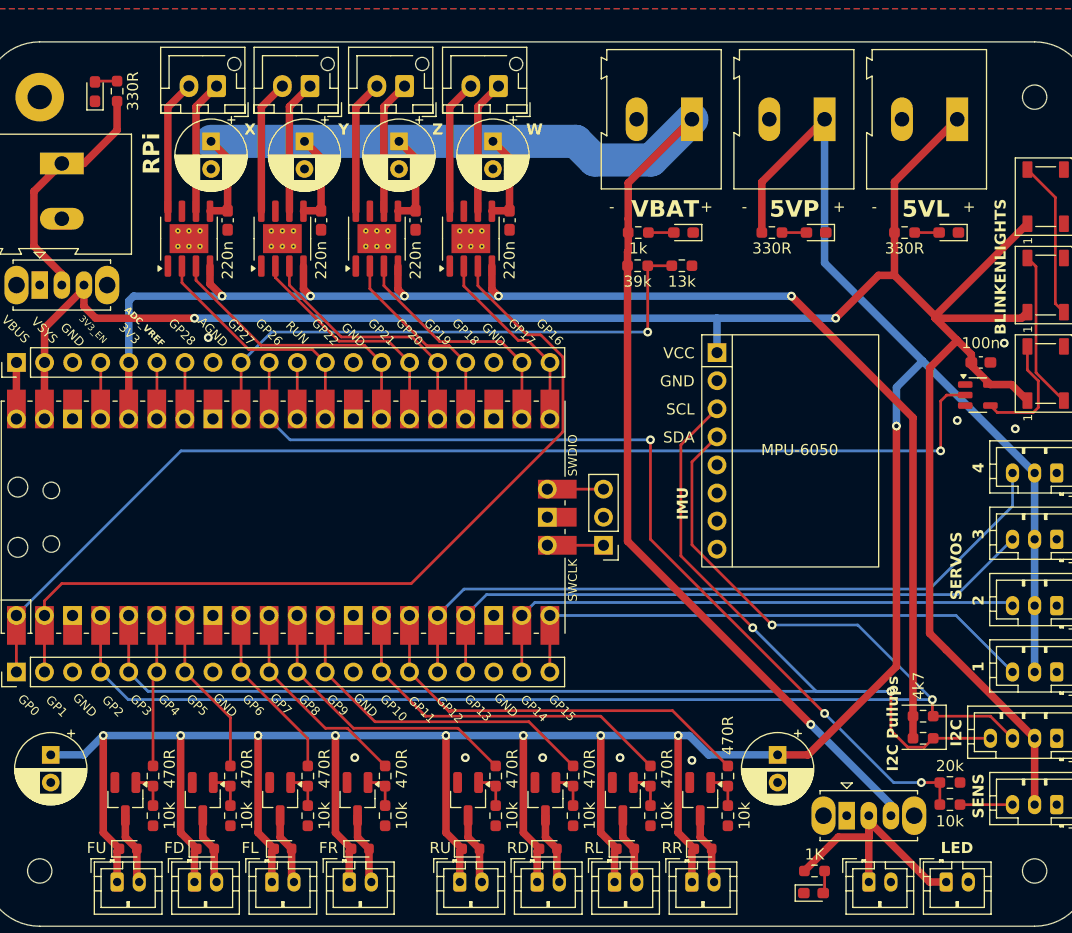
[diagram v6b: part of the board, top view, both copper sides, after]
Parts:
- C1, C11, C2, C5, C7, C9: value 100uF -> 100u
- C10, C4, C6, C8: value 0.22uF -> 220n
- C3: value 0.1uF -> 100n
- R1, R10, R11, R12, R2, R3, R4, R9: value 470 -> 470R
- R17, R18: value 4.7K -> 4k7
- R19: value 10K -> 10k
- R20: value 20K -> 20k
- R21: value 1K -> 1k
- R22, R23, R26: value 330 -> 330R
